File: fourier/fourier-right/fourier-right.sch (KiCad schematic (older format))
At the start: 68 parts, among them J1 VCC, J3 RGB, J6 C6, J7 GND, T1 TRRS, U1 ProMicro

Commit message: Added 1u support on bottom-left, stepped 1.25u support on right half
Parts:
- removed T1: TRRS, Keebio-Parts:TRRS-PJ-320A, symbol TRRS
- added SW_Bb7: SW_PUSH, MX_Alps_Hybrid:MX-1.25U-NoLED, symbol fourier-right-rescue:SW_PUSH-RESCUE-fourier-right
- added U2: TRRS, Keebio-Parts:TRRS-PJ-320A, symbol keebio:TRRS
- D_A1, D_A2, D_A3, D_A4, D_A5, D_A6, D_A7, D_B1, D_B2, D_B3, D_B4, D_B5, D_B7, D_C1, D_C3, D_C4, D_C5, D_C6, D_C7, D_D1, D_D4, D_D5, D_D6, D_D7: footprint Keebio-Parts:Diode-dual -> Keebio-Parts:Diode-Hybrid-Back; symbol D -> device:D
- J1, J3, J6, J7, W2: symbol TEST_1P -> fourier-right-rescue:TEST_1P-RESCUE-fourier-right
- SW_A1, SW_A2, SW_A3, SW_A4, SW_A5, SW_A6, SW_A7, SW_Ab7, SW_B1, SW_B2, SW_B3, SW_B4, SW_B5, SW_B7, SW_C1, SW_C3, SW_C4, SW_C5, SW_C6, SW_C7, SW_Cb6, SW_Cb7, SW_Cc7, SW_D4, SW_D5, SW_D6, SW_D7, SW_Db4, SW_Db5, SW_Db6, SW_Db7, SW_Dc5, SW_Dc6, SW_Dc7, SW_RST1: symbol SW_PUSH -> fourier-right-rescue:SW_PUSH-RESCUE-fourier-right
- SW_D1: footprint MX_Alps_Hybrid:MX-2.25U-NoLED -> MX_Alps_Hybrid:MX-2.25U-ReversedStabilizer-NoLED; symbol SW_PUSH -> fourier-right-rescue:SW_PUSH-RESCUE-fourier-right
- SW_Db1: footprint MX_Alps_Hybrid:MX-2.75U-NoLED -> MX_Alps_Hybrid:MX-2.75U-ReversedStabilizer-NoLED; symbol SW_PUSH -> fourier-right-rescue:SW_PUSH-RESCUE-fourier-right
- U1: symbol ProMicro -> promicro:ProMicro
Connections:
- wire segments 32 -> 79

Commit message: Update footprints
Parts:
- SW_D1: footprint MX_Alps_Hybrid:MX-2.25U-ReversedStabilizer-NoLED -> MX_Alps_Hybrid:MX-2.25U-ReversedStabilizers-NoLED
- SW_Db1: footprint MX_Alps_Hybrid:MX-2.75U-ReversedStabilizer-NoLED -> MX_Alps_Hybrid:MX-2.75U-ReversedStabilizers-NoLED
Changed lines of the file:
@@
 F 0 "SW_D1" H 4350 5610 50  0000 C CNN
 F 1 "SW_PUSH" H 4200 5420 50  0000 C CNN
-F 2 "MX_Alps_Hybrid:MX-2.25U-ReversedStabilizer-NoLED" H 4200 5500 50  0001 C CNN
+F 2 "MX_Alps_Hybrid:MX-2.25U-ReversedStabilizers-NoLED" H 4200 5500 50  0001 C CNN
 F 3 "" H 4200 5500 50  0000 C CNN
 	1    4200 5500
@@
 F 0 "SW_Db1" H 4350 5910 50  0000 C CNN
 F 1 "SW_PUSH" H 4200 5720 50  0000 C CNN
-F 2 "MX_Alps_Hybrid:MX-2.75U-ReversedStabilizer-NoLED" H 4200 5800 50  0001 C CNN
+F 2 "MX_Alps_Hybrid:MX-2.75U-ReversedStabilizers-NoLED" H 4200 5800 50  0001 C CNN
 F 3 "" H 4200 5800 50  0000 C CNN
 	1    4200 5800

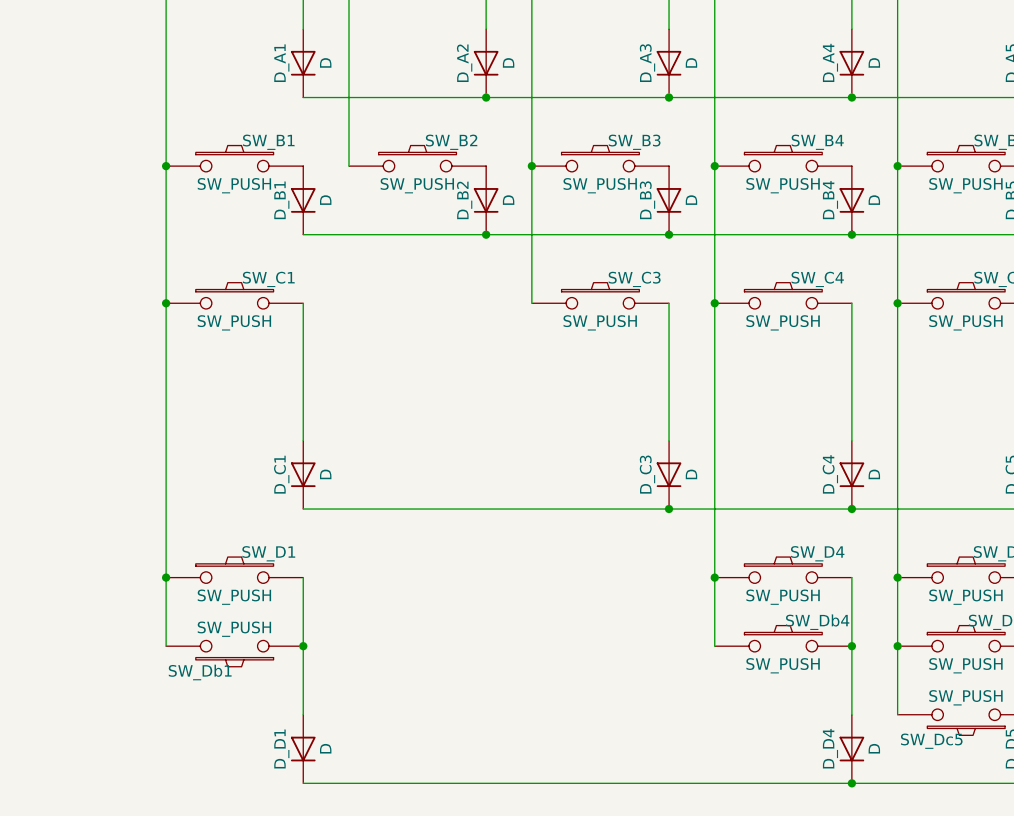
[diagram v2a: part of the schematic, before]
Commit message: Add 1/1.25u inner key option
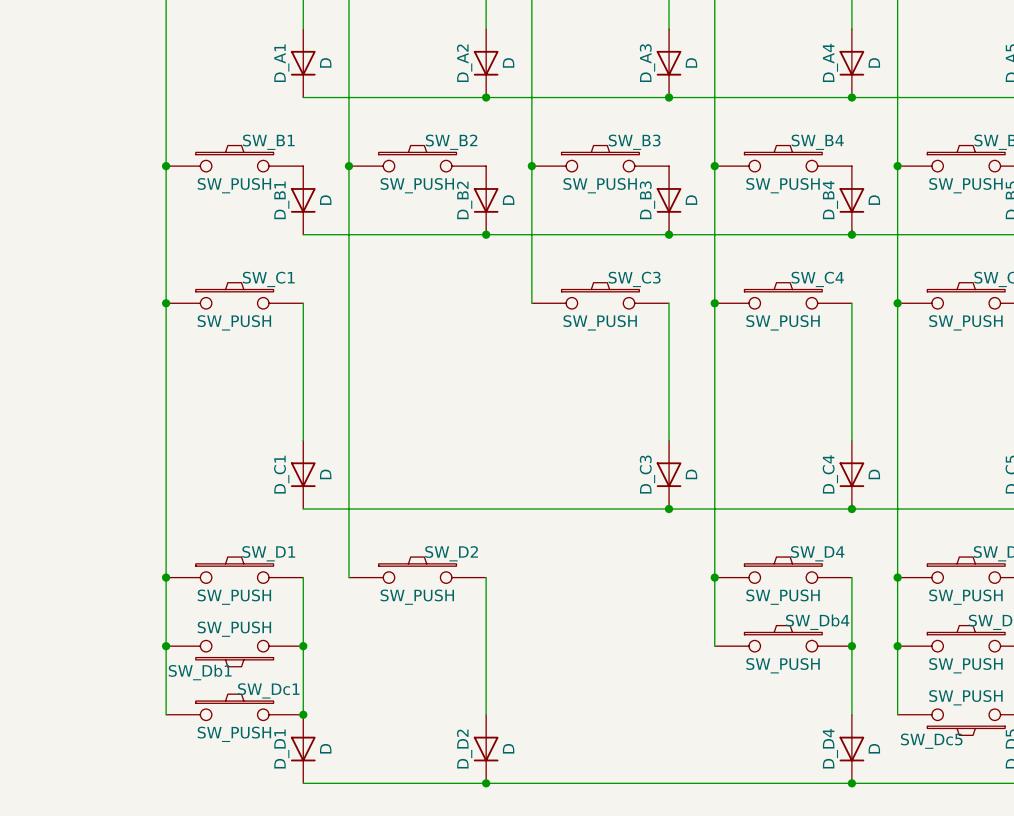
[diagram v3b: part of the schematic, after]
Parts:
- added D_D2: D, Keebio-Parts:Diode-Hybrid-Back, symbol device:D
- added SW_D2: SW_PUSH, MX_Alps_Hybrid:MX-1U-NoLED, symbol fourier-right-rescue:SW_PUSH-RESCUE-fourier-right
- added SW_Dc1: SW_PUSH, MX_Alps_Hybrid:MX-1.25U-NoLED, symbol fourier-right-rescue:SW_PUSH-RESCUE-fourier-right
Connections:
- net col1: now also SW_Dc1.1
- net col2: now also SW_D2.1
- net rowD: now also D_D2.1 (K)
- net at D_D1.2 (A), SW_D1.2, SW_Db1.1: now also SW_Dc1.2
- new net: D_D2.2 (A), SW_D2.2
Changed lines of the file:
@@
 	7700 5500 7700 5800
 Wire Wire Line
-	4500 6400 6900 6400
+	4500 6400 5300 6400
 Connection ~ 9300 5800
 Connection ~ 8700 5800
@@
 	1    0    0    -1
 $EndComp
+$Comp
+L fourier-right-rescue:SW_PUSH-RESCUE-fourier-right SW_Dc1
+U 1 1 5B35297B
+P 4200 6100
+F 0 "SW_Dc1" H 4350 6210 50  0000 C CNN
+F 1 "SW_PUSH" H 4200 6020 50  0000 C CNN
+F 2 "MX_Alps_Hybrid:MX-1.25U-NoLED" H 4200 6100 50  0001 C CNN
+F 3 "" H 4200 6100 50  0000 C CNN
+	1    4200 6100
+	1    0    0    -1
+$EndComp
+Connection ~ 4500 6100
+Wire Wire Line
+	3900 6100 3900 5800
+Connection ~ 3900 5800
+$Comp
+L fourier-right-rescue:SW_PUSH-RESCUE-fourier-right SW_D2
+U 1 1 5B354A43
+P 5000 5500
+F 0 "SW_D2" H 5150 5610 50  0000 C CNN
+F 1 "SW_PUSH" H 5000 5420 50  0000 C CNN
+F 2 "MX_Alps_Hybrid:MX-1U-NoLED" H 5000 5500 50  0001 C CNN
+F 3 "" H 5000 5500 50  0000 C CNN
+	1    5000 5500
+	1    0    0    -1
+$EndComp
+$Comp
+L device:D D_D2
+U 1 1 5B354BFF
+P 5300 6250
+F 0 "D_D2" H 5300 6350 50  0000 C CNN
+F 1 "D" H 5300 6150 50  0000 C CNN
+F 2 "Keebio-Parts:Diode-Hybrid-Back" H 5300 6250 50  0001 C CNN
+F 3 "" H 5300 6250 50  0001 C CNN
+	1    5300 6250
+	0    -1   -1   0
+$EndComp
+Connection ~ 5300 6400
+Wire Wire Line
+	5300 6400 6900 6400
+Wire Wire Line
+	5300 6100 5300 5500
+Wire Wire Line
+	4700 5500 4700 3700
+Connection ~ 4700 3700
 $EndSCHEMATC

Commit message: Right side - fix TRRS jack, switch to staggered Pro Micro
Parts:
- U1: footprint Keebio-Parts:ArduinoProMicro -> Keebio-Parts:ArduinoProMicro-ZigZag; symbol promicro:ProMicro -> fourier-right-rescue:ProMicro-promicro
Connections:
- no-connect marks 0 -> 2
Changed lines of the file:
@@
 EESchema Schematic File Version 4
 LIBS:fourier-right-cache
-EELAYER 26 0
+EELAYER 29 0
 EELAYER END
 $Descr USLetter 11000 8500
@@
 Text GLabel 1950 2200 0    60   Input ~ 0
 LED
-$Comp
-L promicro:ProMicro U1
-U 1 1 597A37F8
-P 2650 1650
-F 0 "U1" H 2650 1650 60  0000 C CNN
-F 1 "ProMicro" H 2650 900 60  0000 C CNN
-F 2 "Keebio-Parts:ArduinoProMicro" V 3700 -850 60  0001 C CNN
-F 3 "" V 3700 -850 60  0001 C CNN
-	1    2650 1650
-	1    0    0    -1
-$EndComp
 $Comp
 L fourier-right-rescue:TEST_1P-RESCUE-fourier-right J1
@@
 	9300 3700 9300 3550
 $Comp
-L keebio:TRRS U2
-U 1 1 5A9EF88B
-P 1400 3300
-F 0 "U2" H 1628 3603 60  0000 L CNN
-F 1 "TRRS" H 1628 3497 60  0000 L CNN
-F 2 "Keebio-Parts:TRRS-PJ-320A" H 1550 3300 60  0001 C CNN
-F 3 "" H 1550 3300 60  0001 C CNN
-	1    1400 3300
-	1    0    0    -1
-$EndComp
-$Comp
 L fourier-right-rescue:SW_PUSH-RESCUE-fourier-right SW_Dc1
 U 1 1 5B35297B
@@
 	4700 5500 4700 3700
 Connection ~ 4700 3700
+$Comp
+L fourier-right-rescue:ProMicro-promicro U1
+U 1 1 597A37F8
+P 2650 1650
+F 0 "U1" H 2650 1650 60  0000 C CNN
+F 1 "ProMicro" H 2650 900 60  0000 C CNN
+F 2 "Keebio-Parts:ArduinoProMicro-ZigZag" V 3700 -850 60  0001 C CNN
+F 3 "" V 3700 -850 60  0001 C CNN
+	1    2650 1650
+	1    0    0    -1
+$EndComp
+$Comp
+L keebio:TRRS U2
+U 1 1 5C4F55F1
+P 1400 3300
+F 0 "U2" H 1628 3603 60  0000 L CNN
+F 1 "TRRS" H 1628 3497 60  0000 L CNN
+F 2 "Keebio-Parts:TRRS-PJ-320A" H 1550 3300 60  0001 C CNN
+F 3 "" H 1550 3300 60  0001 C CNN
+	1    1400 3300
+	1    0    0    -1
+$EndComp
+NoConn ~ 3350 1100
+NoConn ~ 1950 1700
 $EndSCHEMATC
